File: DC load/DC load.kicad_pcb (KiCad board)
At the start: 2 copper layers, 100 x 88.9 mm, 26 parts, among them J1 CTL IN, J2 CTL OUT, J3 B+, J4 B-, M1 3.2mm, M2 3.2mm, M3 3.2mm, Q1 IRFI540, U1 LM324

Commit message: Some layout stuff
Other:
- board text added: "FEF/DTU"
- board text added: "v1.0 2019"
- board text removed: "FEF 2019"
- board text removed: "v1.0"

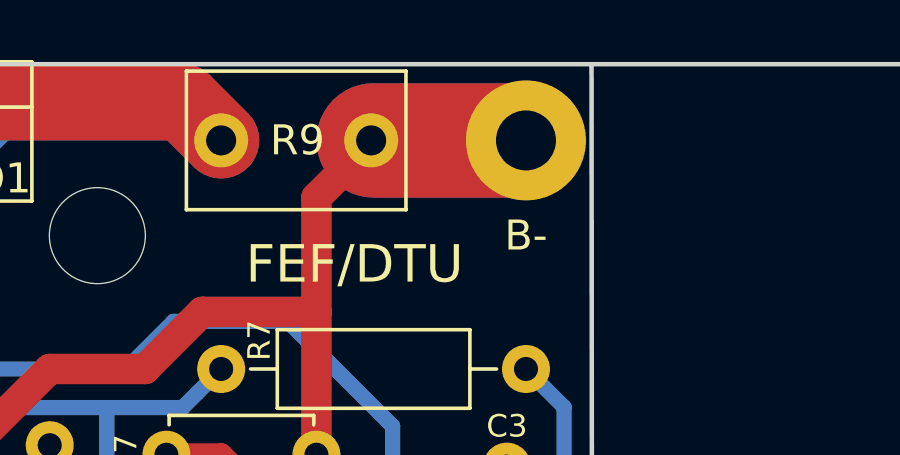
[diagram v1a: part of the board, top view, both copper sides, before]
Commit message: Small layout fix
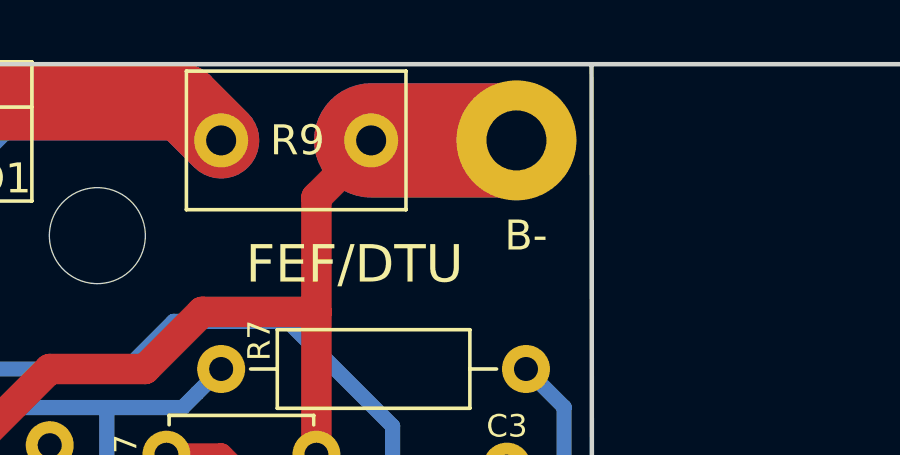
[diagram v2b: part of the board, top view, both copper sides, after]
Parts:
- moved J4 0.32 mm to (64.1, 35.9)
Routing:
- net GND: track 92.3 -> 91.4 mm
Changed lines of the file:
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@@
     (links 44)
     (no_connects 0)
-    (area 33.262499 33.262499 133.412501 122.312501)
+    (area 32.919999 32.902499 133.412501 122.312501)
     (thickness 1.6)
     (drawings 29)
-    (tracks 192)
+    (tracks 190)
     (zones 0)
     (modules 26)
@@
   )
   (setup
-    (last_trace_width 0.25)
+    (last_trace_width 3.81)
     (user_trace_width 0.254)
     (user_trace_width 0.381)
@@
     (zone_45_only no)
     (trace_min 0.2)
-    (segment_width 2.54)
+    (segment_width 3.81)
     (edge_width 0.15)
     (via_size 0.6)
@@
     (pad_to_mask_clearance 0.2)
     (aux_axis_origin 0 0)
-    (grid_origin 33.3375 33.3375)
-    (visible_elements 7FFFEFFF)
+    (visible_elements 7FFFFFFF)
     (pcbplotparams
       (layerselection 0x00030_80000001)
@@
   )
   (module Wire_Pads:SolderWirePad_single_2-5mmDrill (layer F.Cu)
-    (at 64.4525 35.8775)
+    (at 64.135 35.8775)
     (fp_text reference J4 (at 0.635 3.175) (layer F.SilkS) hide
       (effects (font (size 1 1) (thickness 0.15)))
@@
     )
   )
+  (gr_line (start 64.135 35.8775) (end 59.2925 35.8775) (layer F.Mask) (width 3.81))
   (gr_text B- (at 64.4525 39.0525) (layer F.SilkS)
     (effects (font (size 1 1) (thickness 0.15)))
@@
     (effects (font (size 1.25 1.25) (thickness 0.3)))
   )
-  (gr_line (start 59.3725 35.8775) (end 64.4525 35.8775) (layer B.Mask) (width 3.81))
+  (gr_line (start 59.2925 35.8775) (end 64.135 35.8775) (layer B.Mask) (width 3.81))
   (gr_line (start 53.0225 34.6075) (end 54.2925 35.8775) (layer B.Mask) (width 2.54))
   (gr_line (start 46.6725 34.6075) (end 53.0225 34.6075) (layer B.Mask) (width 2.54))
@@
   (gr_line (start 46.6725 34.6075) (end 53.0225 34.6075) (layer F.Mask) (width 2.54))
   (gr_line (start 45.4025 35.8775) (end 46.6725 34.6075) (layer F.Mask) (width 2.032))
-  (gr_line (start 59.3725 35.8775) (end 64.4525 35.8775) (layer F.Mask) (width 3.81))
   (gr_line (start 42.8625 37.7825) (end 42.8625 35.8775) (layer F.Mask) (width 2.54))
   (gr_line (start 41.5925 39.0525) (end 42.8625 37.7825) (layer F.Mask) (width 2.54))
@@
   (gr_line (start 33.3375 33.3375) (end 33.3375 122.2375) (layer Edge.Cuts) (width 0.15))
   (gr_line (start 33.3375 33.3375) (end 133.3375 33.3375) (layer Edge.Cuts) (width 0.15))
+  (segment (start 59.2925 35.8775) (end 64.135 35.8775) (width 3.81) (layer B.Cu) (net 1))
+  (segment (start 59.2925 35.8775) (end 64.135 35.8775) (width 3.81) (layer F.Cu) (net 1))
   (segment (start 57.5475 66.9925) (end 57.5475 61.4325) (width 1.016) (layer F.Cu) (net 1))
   (segment (start 57.5475 61.4325) (end 59.6075 59.3725) (width 1.016) (layer F.Cu) (net 1))
@@
   (segment (start 57.4675 37.7825) (end 59.3725 35.8775) (width 1.016) (layer F.Cu) (net 1) (status 20))
   (segment (start 38.4175 68.8975) (end 38.4975 68.8975) (width 0.762) (layer F.Cu) (net 1) (status 30))
-  (segment (start 59.3725 35.8775) (end 64.4525 35.8775) (width 3.81) (layer F.Cu) (net 1) (status 30))
-  (segment (start 59.3725 35.8775) (end 62.23 35.8775) (width 3.81) (layer B.Cu) (net 1) (status 10))
-  (segment (start 62.23 35.8775) (end 64.4525 35.8775) (width 3.81) (layer B.Cu) (net 1) (status 20))
-  (segment (start 62.5475 36.195) (end 62.23 35.8775) (width 0.508) (layer B.Cu) (net 1) (status 10))
   (segment (start 48.5775 68.8975) (end 48.5775 65.0875) (width 0.508) (layer B.Cu) (net 2) (status 30))
   (segment (start 48.5775 62.5475) (end 51.7525 59.3725) (width 0.508) (layer B.Cu) (net 2) (status 30))
